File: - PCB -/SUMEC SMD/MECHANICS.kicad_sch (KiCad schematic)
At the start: 7 parts, among them J1 Conn_01x04_Pin, SW1 SW_SPDT, SW3 SW_Push

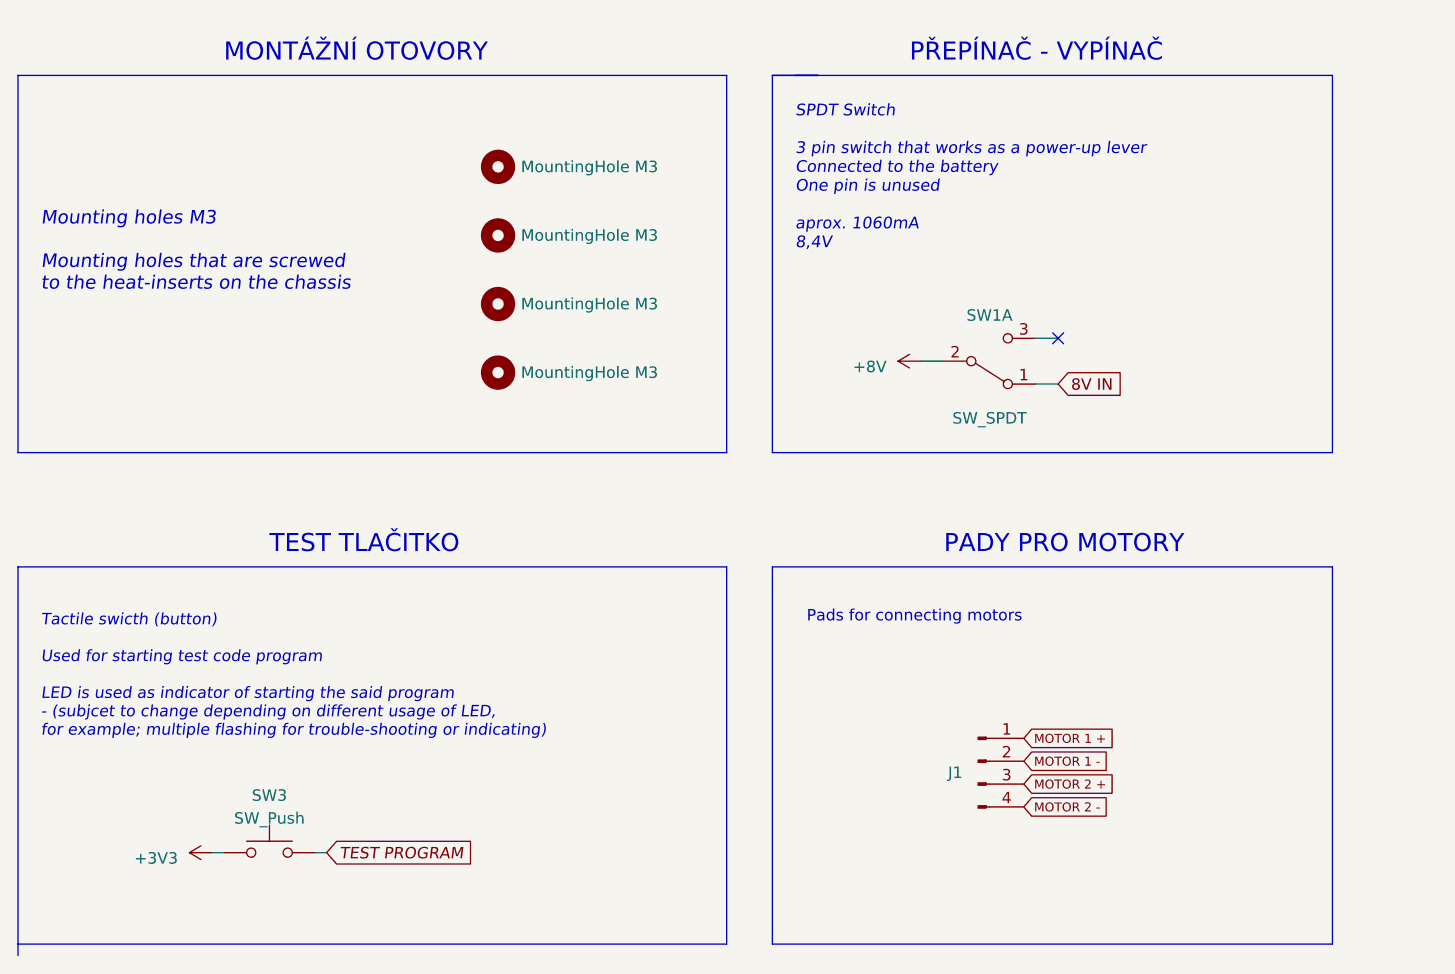
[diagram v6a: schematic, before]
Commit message: PCB cooler schematic and start of board making
bettr cal sol
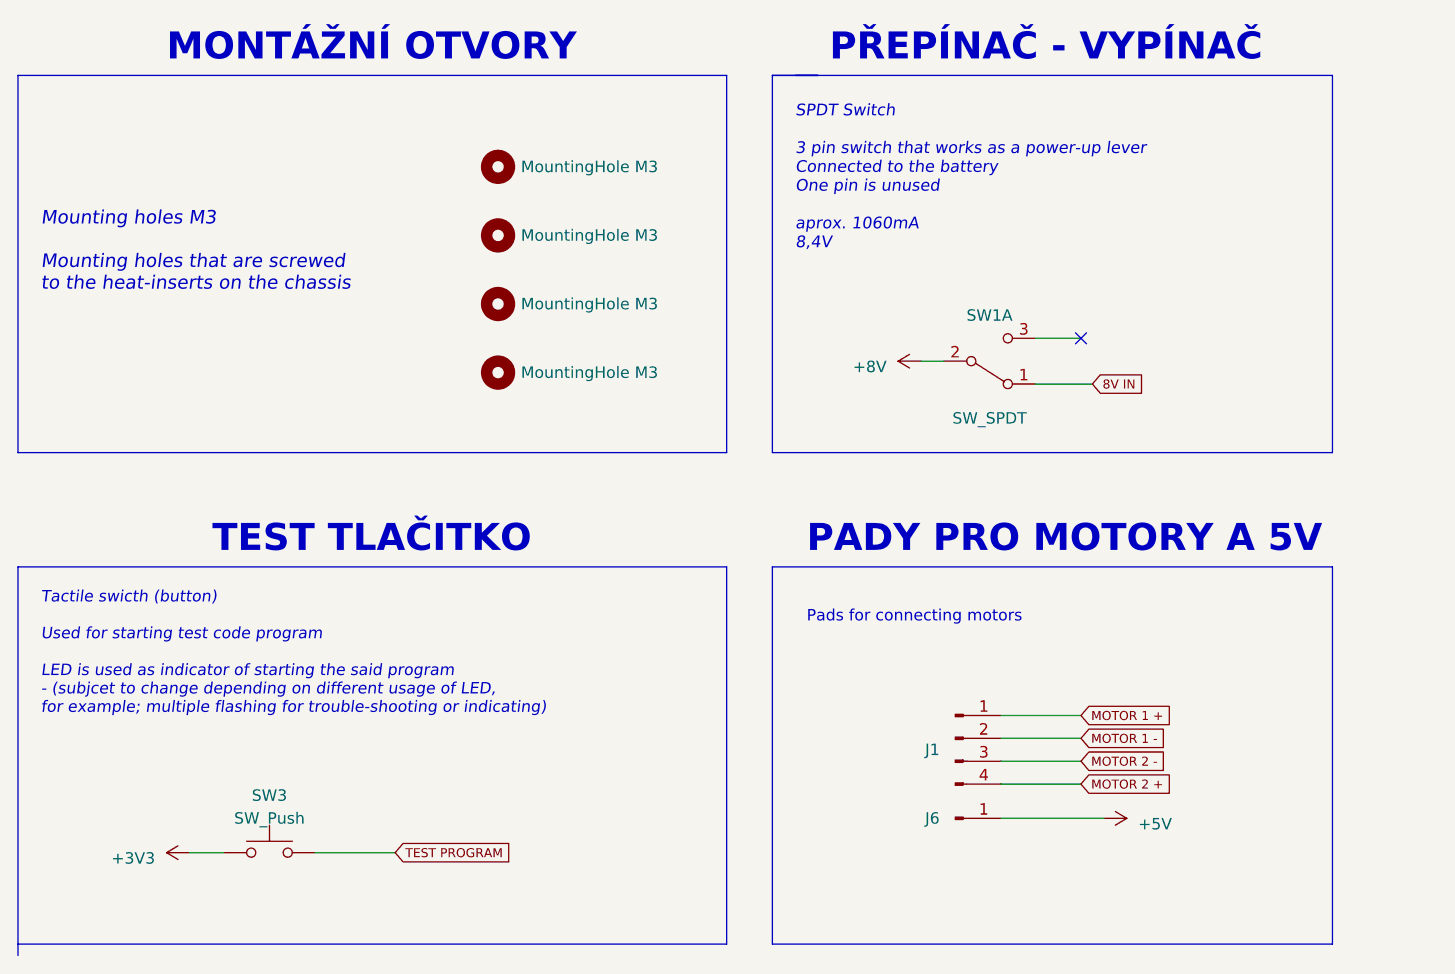
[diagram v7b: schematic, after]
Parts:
- added J6: Conn_01x01_Pin, Connector_Wire:SolderWire-0.1sqmm_1x01_D0.4mm_OD1mm, symbol Connector:Conn_01x01_Pin
- SW3: footprint Button_Switch_SMD:SW_SPST_B3U-1000P -> Button_Switch_THT:SW_PUSH_6mm
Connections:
- net MOTOR 2 +: now also J1.4 (Pin_4); no longer J1.3 (Pin_3)
- net MOTOR 2 -: now also J1.3 (Pin_3); no longer J1.4 (Pin_4)
- new net +5V: J6.1 (Pin_1)
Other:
- note added: "MONTÁŽNÍ OTVORY"
- note added: "PADY PRO MOTORY A 5V"
- note removed: "MONTÁŽNÍ OTOVORY"
- note removed: "PADY PRO MOTORY"
